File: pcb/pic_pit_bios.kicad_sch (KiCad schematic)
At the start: 16 parts, among them J15 PC SPK, U10 8259A-2, U9 8254

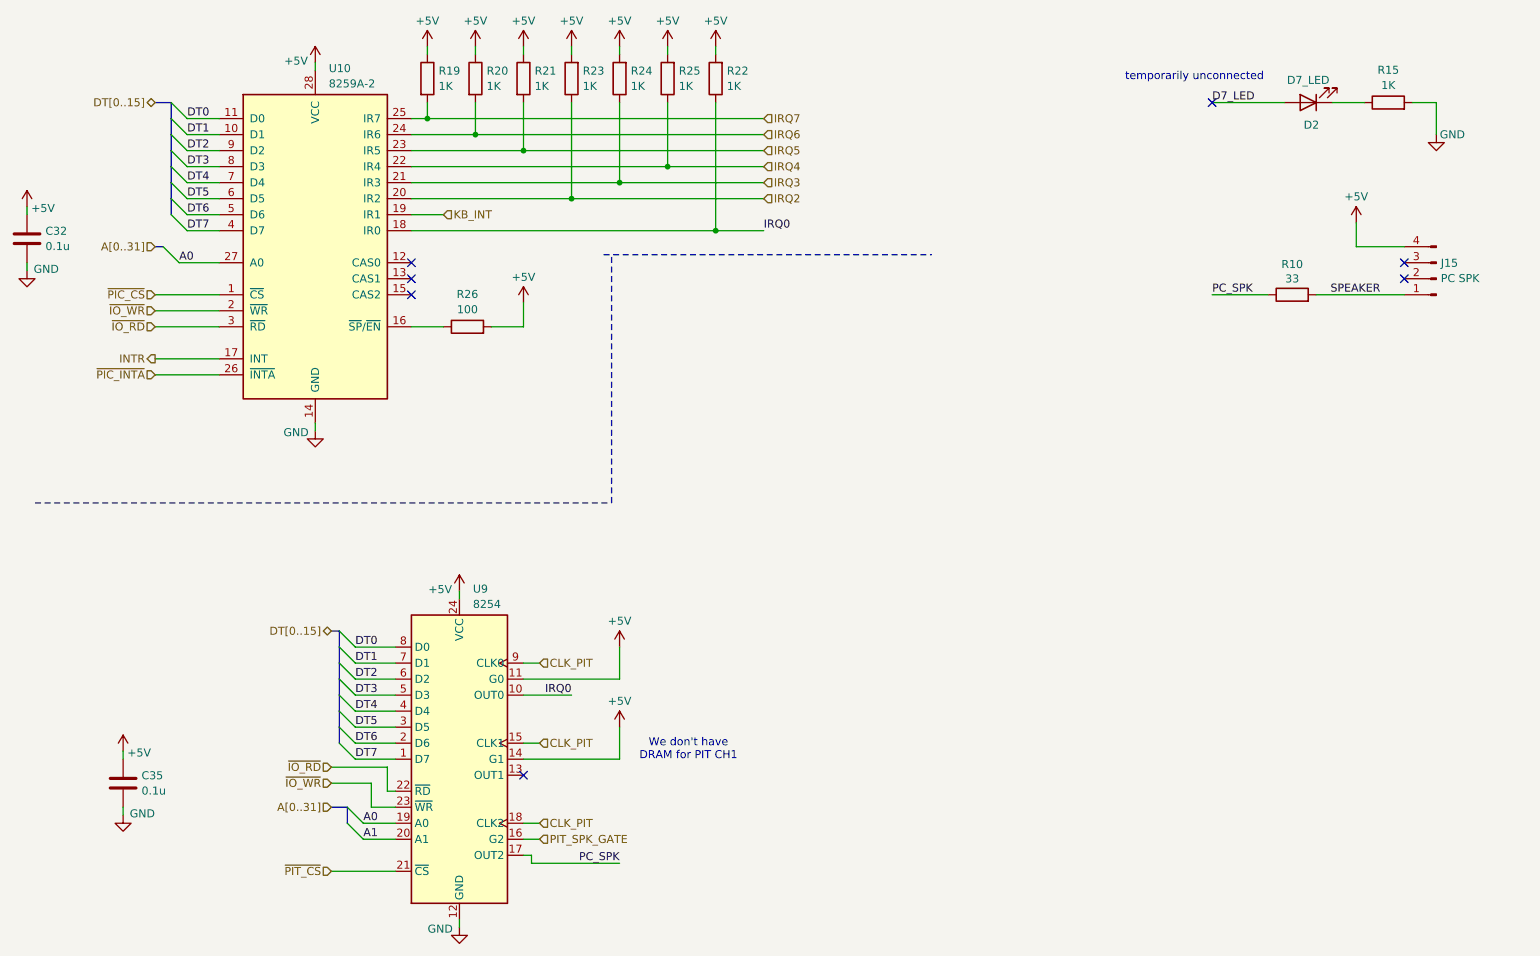
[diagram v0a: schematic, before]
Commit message: moving BIOS to slow SA/DT side of CPU bus
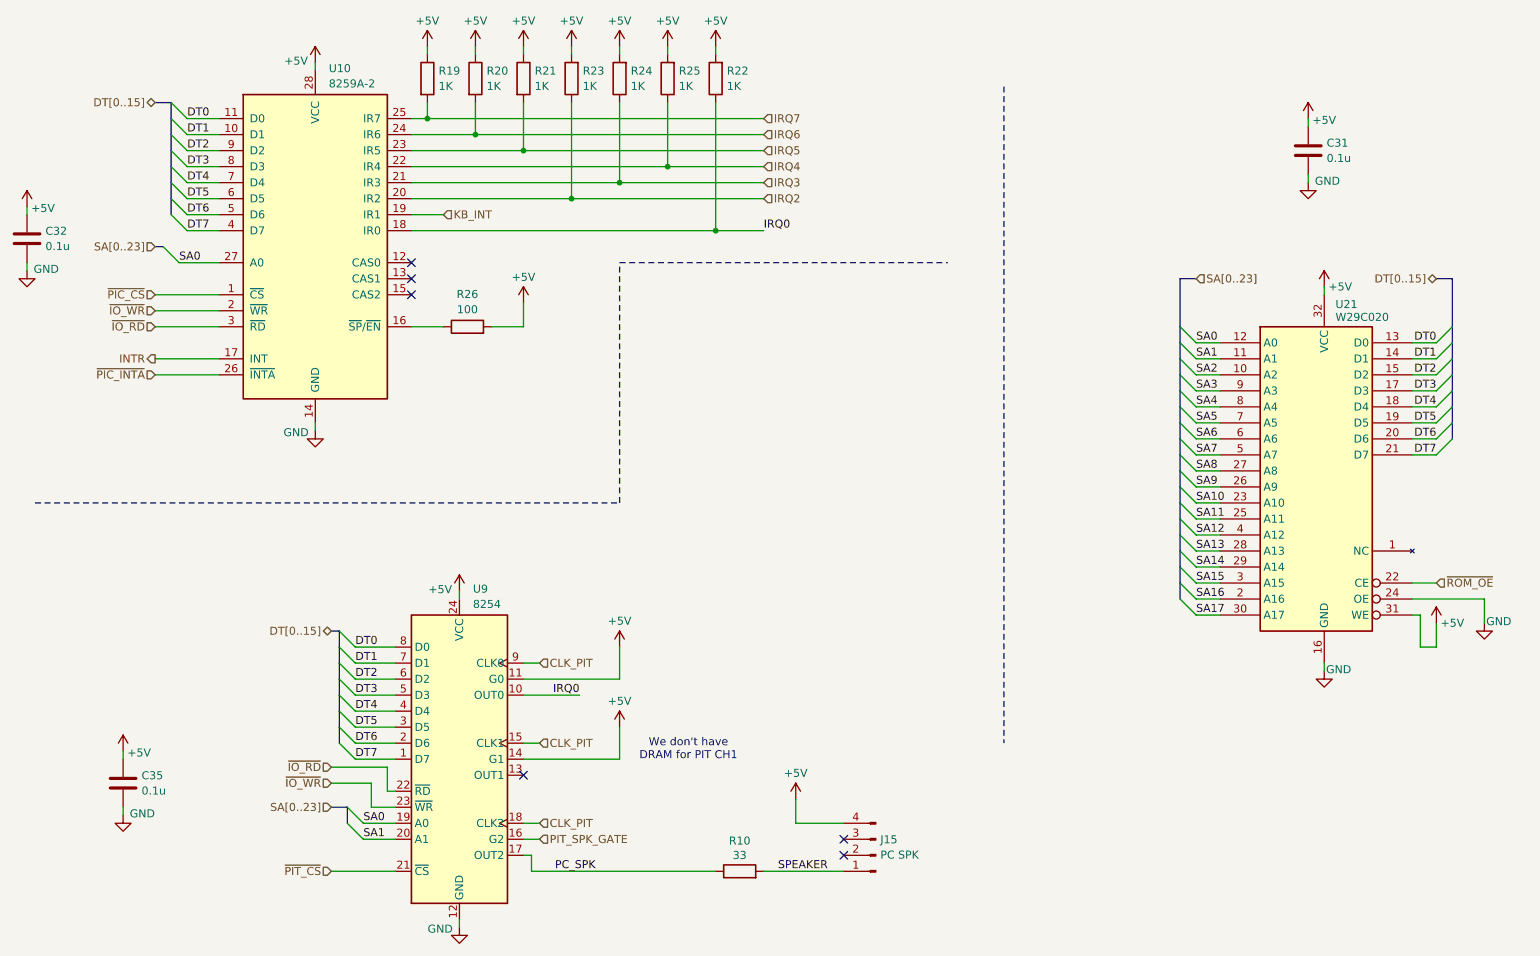
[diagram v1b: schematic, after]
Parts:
- removed D2: D7_LED, LED_THT:LED_D4.0mm, symbol Device:LED
- removed R15: 1K, Resistor_SMD:R_0805_2012Metric_Pad1.20x1.40mm_HandSolder, symbol Device:R
- added C31: 0.1u, Capacitor_SMD:C_0805_2012Metric_Pad1.18x1.45mm_HandSolder, symbol Device:C
- added U21: W29C020, Package_DIP:DIP-32_W15.24mm, symbol sbc486_additional:W29C020
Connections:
- net +5V: now also C31.2, U21.31 (WE), U21.32 (VCC)
- net DT0: now also U21.13 (D0)
- net DT1: now also U21.14 (D1)
- net DT2: now also U21.15 (D2)
- net DT3: now also U21.17 (D3)
- net DT4: now also U21.18 (D4)
- net DT5: now also U21.19 (D5)
- net DT6: now also U21.20 (D6)
- net DT7: now also U21.21 (D7)
- net GND: now also C31.1, U21.16 (GND), U21.24 (OE)
- net A0 renamed SA0
- net SA0: now also U21.12 (A0)
- net A1 renamed SA1
- net SA1: now also U21.11 (A1)
- new net SA10: U21.23 (A10)
- new net SA11: U21.25 (A11)
- new net SA12: U21.4 (A12)
- new net SA13: U21.28 (A13)
- new net SA14: U21.29 (A14)
- new net SA15: U21.3 (A15)
- new net SA16: U21.2 (A16)
- new net SA17: U21.30 (A17)
- new net SA2: U21.10 (A2)
- new net SA3: U21.9 (A3)
- new net SA4: U21.8 (A4)
- new net SA5: U21.7 (A5)
- new net SA6: U21.6 (A6)
- new net SA7: U21.5 (A7)
- new net SA8: U21.27 (A8)
- new net SA9: U21.26 (A9)
- new net ~{ROM_OE}: U21.22 (CE)
- no-connect marks 7 -> 6
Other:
- note removed: "temporarily unconnected"
- moved on the sheet: J15, R10

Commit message: unified 10K pullups
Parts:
- R19, R20, R21, R22, R23, R24, R25: value 1K -> 10K
- R26: value 100 -> 10K
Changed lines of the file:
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@@
 		)
 	)
-	(polyline
-		(pts
-			(xy 116.84 63.5) (xy 168.91 63.5)
-		)
-		(stroke
-			(width 0)
-			(type dash)
-		)
-	)
 	(wire
 		(pts
@@
 	(polyline
 		(pts
-			(xy 116.84 101.6) (xy 116.84 63.5)
+			(xy 167.64 101.6) (xy 116.84 101.6)
 		)
 		(stroke
@@
 		)
 	)
+	(polyline
+		(pts
+			(xy 167.64 101.6) (xy 172.72 101.6)
+		)
+		(stroke
+			(width 0)
+			(type dash)
+		)
+	)
 	(wire
 		(pts
@@
 		)
 	)
+	(polyline
+		(pts
+			(xy 177.8 139.7) (xy 177.8 157.48)
+		)
+		(stroke
+			(width 0)
+			(type dash)
+		)
+	)
 	(wire
 		(pts
@@
 		(on_board yes)
 		(dnp no)
-		(fields_autoplaced yes)
 		(property "Reference" "R21"
-			(at 103.378 33.0778 0)
+			(at 103.632 33.02 0)
 			(effects
 				(font
@@
 			)
 		)
-		(property "Value" "1K"
-			(at 103.378 35.5021 0)
+		(property "Value" "10K"
+			(at 103.632 35.56 0)
 			(effects
 				(font
@@
 		(on_board yes)
 		(dnp no)
-		(fields_autoplaced yes)
 		(property "Reference" "R23"
-			(at 110.998 33.0778 0)
+			(at 111.252 33.02 0)
 			(effects
 				(font
@@
 			)
 		)
-		(property "Value" "1K"
-			(at 110.998 35.5021 0)
+		(property "Value" "10K"
+			(at 111.252 35.56 0)
 			(effects
 				(font
@@
 		(on_board yes)
 		(dnp no)
-		(fields_autoplaced yes)
 		(property "Reference" "R22"
-			(at 133.858 33.0778 0)
+			(at 134.112 33.02 0)
 			(effects
 				(font
@@
 			)
 		)
-		(property "Value" "1K"
-			(at 133.858 35.5021 0)
+		(property "Value" "10K"
+			(at 134.112 35.56 0)
 			(effects
 				(font
@@
 		(on_board yes)
 		(dnp no)
-		(fields_autoplaced yes)
 		(property "Reference" "R25"
-			(at 126.238 33.0778 0)
+			(at 126.492 33.02 0)
 			(effects
 				(font
@@
 			)
 		)
-		(property "Value" "1K"
-			(at 126.238 35.5021 0)
+		(property "Value" "10K"
+			(at 126.492 35.56 0)
 			(effects
 				(font
@@
 		(fields_autoplaced yes)
 		(property "Reference" "R26"
-			(at 92.71 68.4995 90)
+			(at 92.71 67.31 90)
 			(effects
 				(font
@@
 			)
 		)
-		(property "Value" "100"
-			(at 92.71 70.9238 90)
+		(property "Value" "10K"
+			(at 92.71 69.85 90)
 			(effects
 				(font
@@
 		(on_board yes)
 		(dnp no)
-		(fields_autoplaced yes)
 		(property "Reference" "R24"
-			(at 118.618 33.0778 0)
+			(at 118.872 33.02 0)
 			(effects
 				(font
@@
 			)
 		)
-		(property "Value" "1K"
-			(at 118.618 35.5021 0)
+		(property "Value" "10K"
+			(at 118.872 35.56 0)
 			(effects
 				(font
@@
 		(on_board yes)
 		(dnp no)
-		(fields_autoplaced yes)
 		(property "Reference" "R19"
-			(at 88.138 33.0778 0)
+			(at 88.392 33.02 0)
 			(effects
 				(font
@@
 			)
 		)
-		(property "Value" "1K"
-			(at 88.138 35.5021 0)
+		(property "Value" "10K"
+			(at 88.392 35.56 0)
 			(effects
 				(font
@@
 		(on_board yes)
 		(dnp no)
-		(fields_autoplaced yes)
 		(property "Reference" "R20"
-			(at 95.758 33.0778 0)
+			(at 96.012 33.02 0)
 			(effects
 				(font
@@
 			)
 		)
-		(property "Value" "1K"
-			(at 95.758 35.5021 0)
+		(property "Value" "10K"
+			(at 96.012 35.56 0)
 			(effects
 				(font

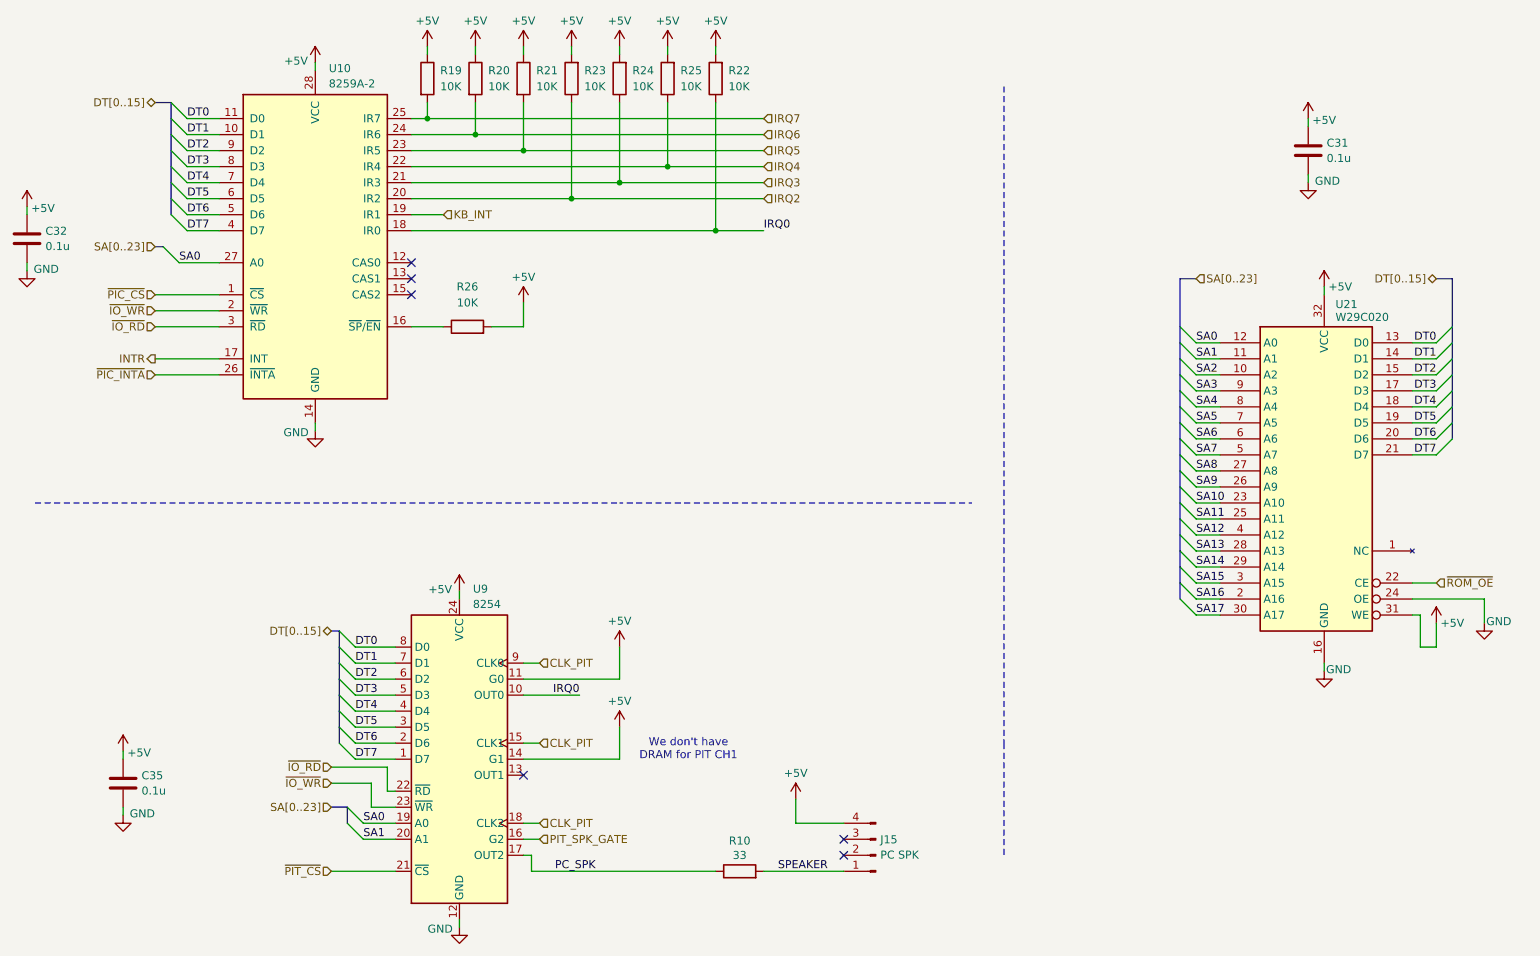
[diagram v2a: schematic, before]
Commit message: dropping cap, cosmetics
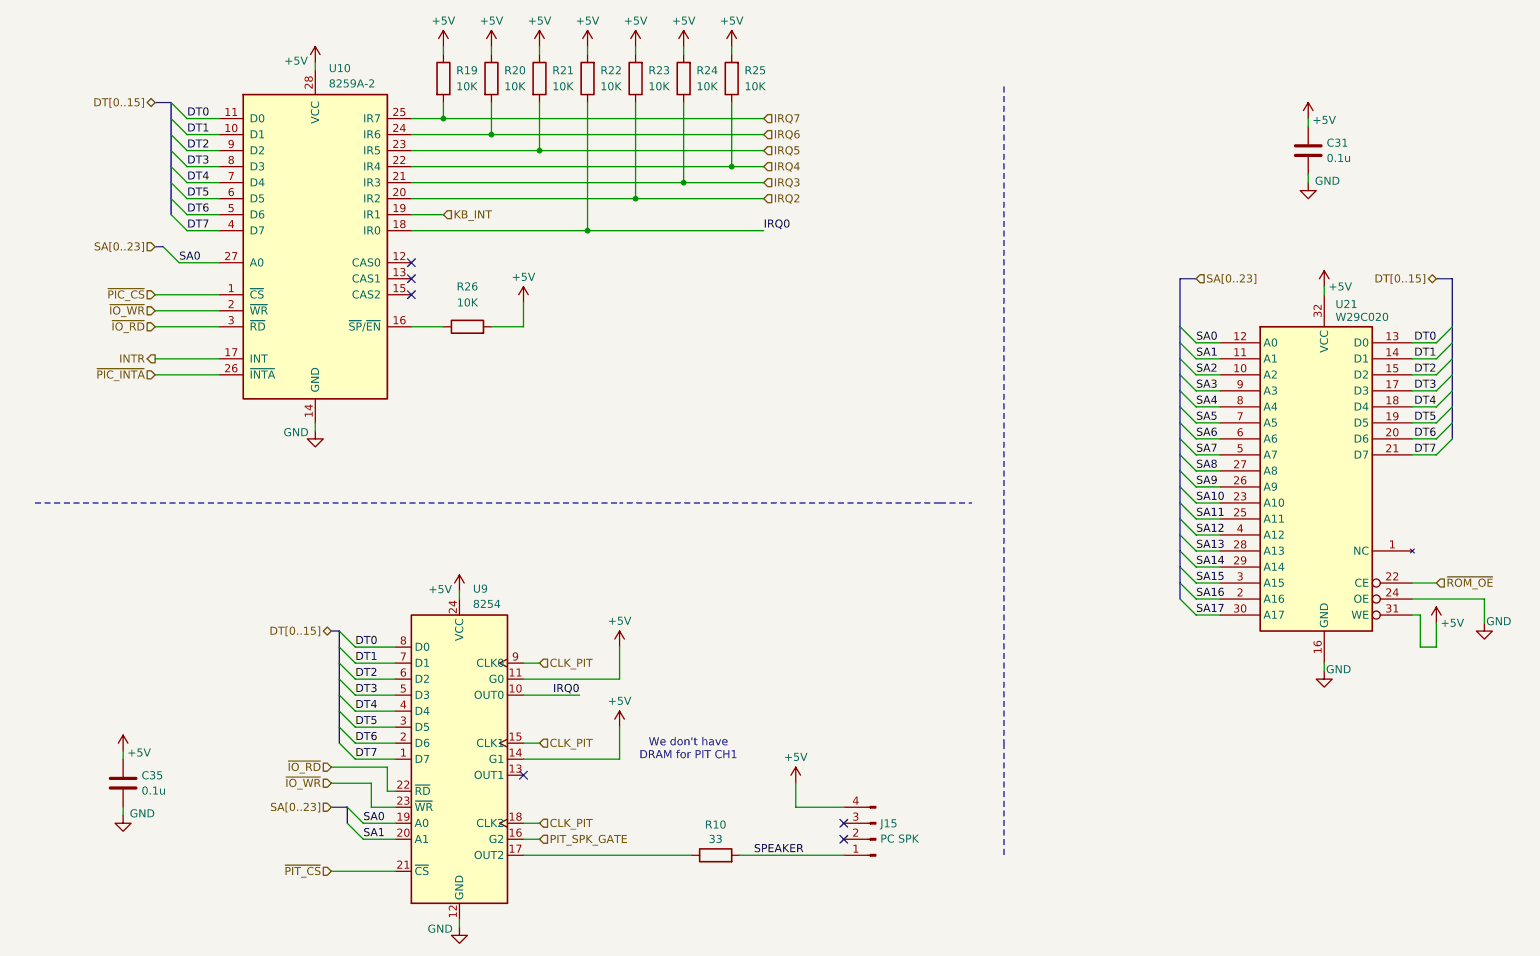
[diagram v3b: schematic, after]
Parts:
- removed C32: 0.1u, Capacitor_SMD:C_0805_2012Metric_Pad1.18x1.45mm_HandSolder, symbol Device:C
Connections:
- net PC_SPK: no longer names the net of R10.1, U9.17 (OUT2)
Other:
- moved on the sheet: J15, R10, R19, R20, R21, R22, R23, R24, R25
